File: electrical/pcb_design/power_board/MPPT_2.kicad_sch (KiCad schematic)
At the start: 14 parts

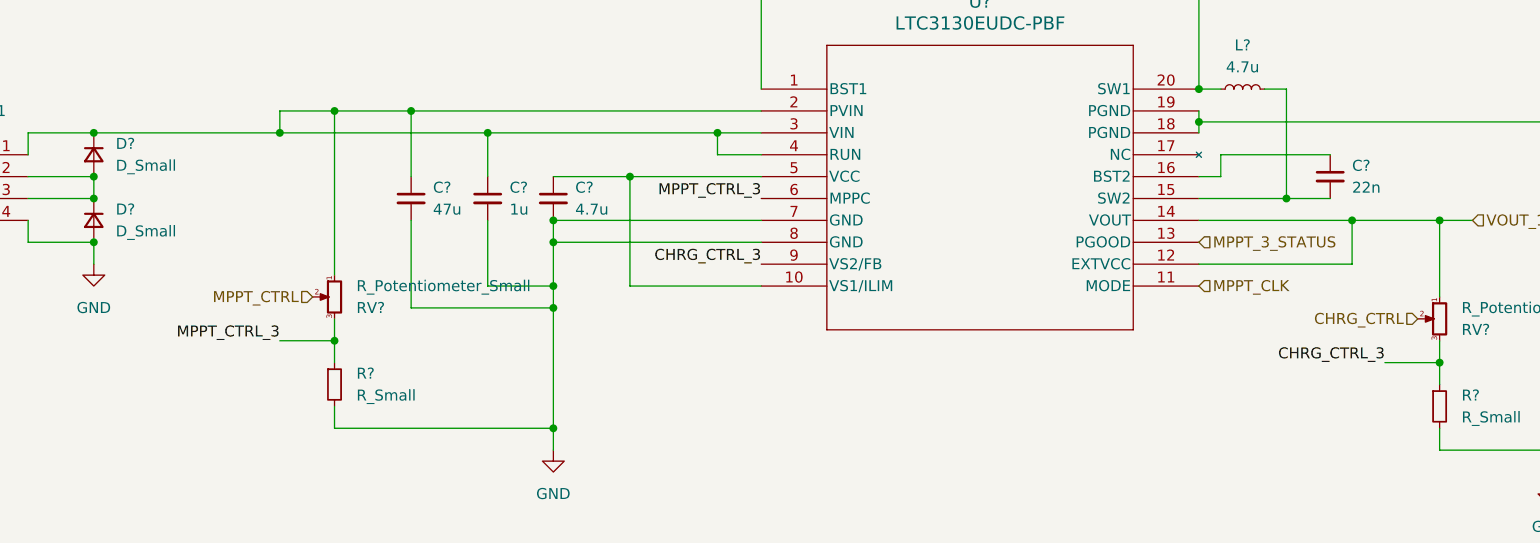
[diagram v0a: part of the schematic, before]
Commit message: missing sense and set hw
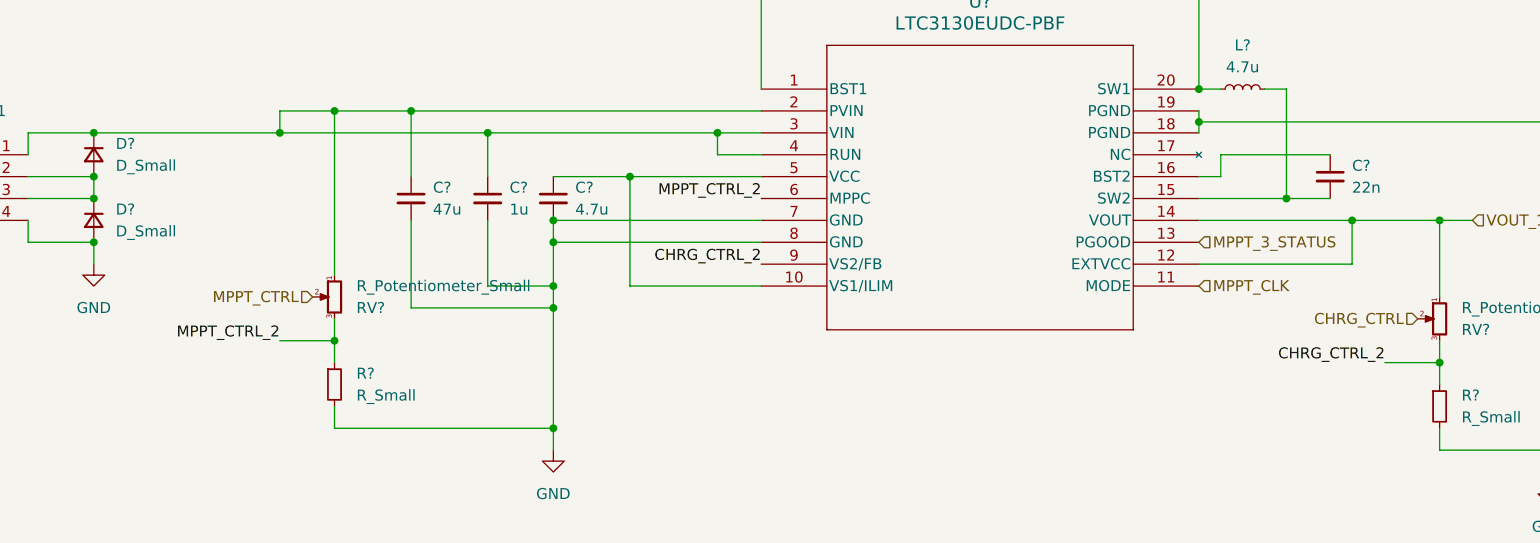
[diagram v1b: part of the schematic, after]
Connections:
- net CHRG_CTRL_3 renamed CHRG_CTRL_2
- net MPPT_CTRL_3 renamed MPPT_CTRL_2

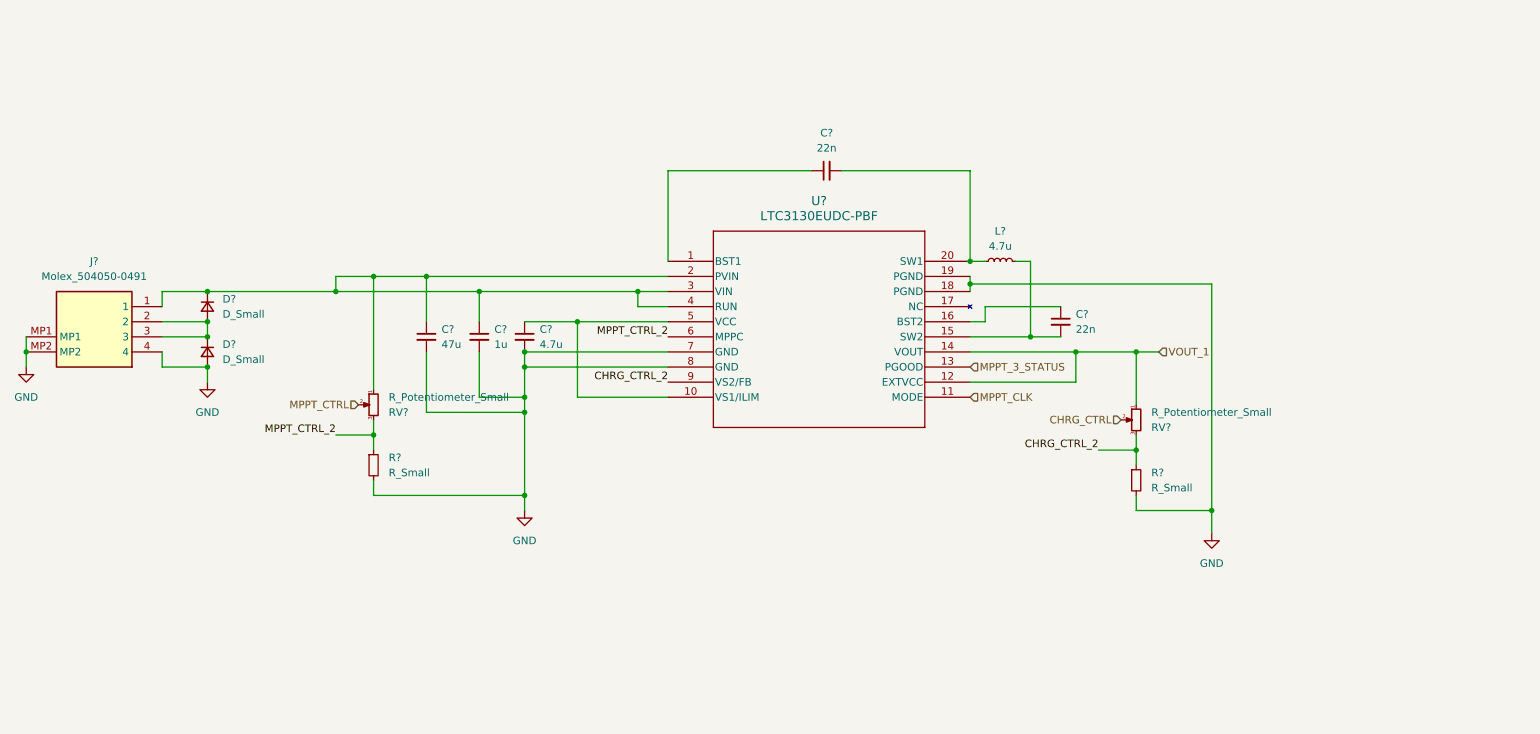
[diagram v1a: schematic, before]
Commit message: power board schematic first draft but missing some resistor and diode specs, and smart mcu pinout
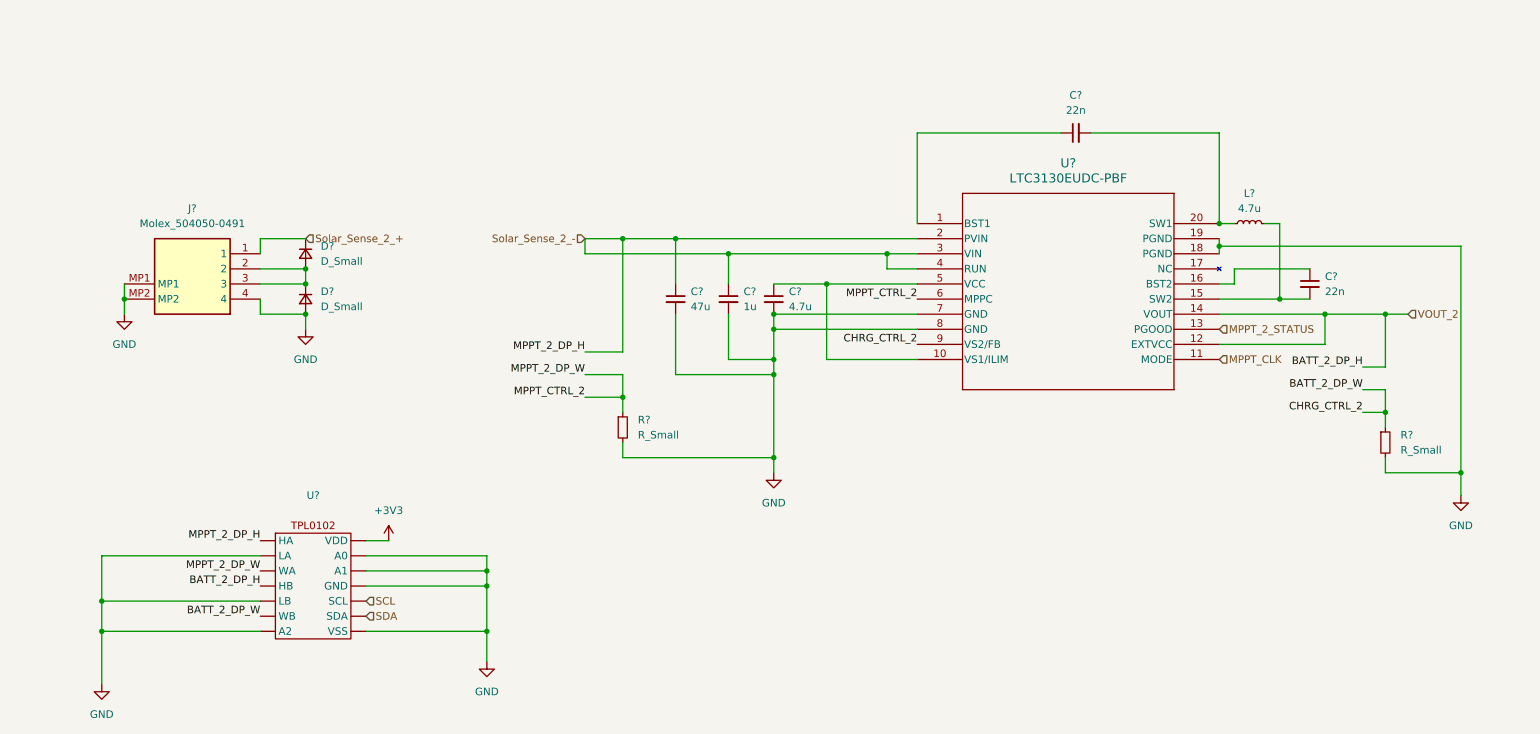
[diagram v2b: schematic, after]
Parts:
- removed C?: 47u, symbol Device:C_Small
- removed C? (x2): 22n, symbol Device:C_Small
- removed C?: 4.7u, symbol Device:C_Small
- removed C?: 1u, symbol Device:C_Small
- removed D? (x2): D_Small, symbol Device:D_Small
- removed J?: Molex_504050-0491, footprints:Molex_504050-0491, symbol tvsc_symbols:Molex_504050-0491
- removed L?: 4.7u, symbol Device:L_Small
- removed R? (x2): R_Small, symbol Device:R_Small
- removed RV? (x2): R_Potentiometer_Small, symbol Device:R_Potentiometer_Small
- removed U?: LTC3130EUDC-PBF, UDC_20_ADI, symbol LTC3130:LTC3130EUDC-PBF
- added C?: 47u, symbol Device:C_Small
- added C?: 1u, symbol Device:C_Small
- added C? (x2): 22n, symbol Device:C_Small
- added C?: 4.7u, symbol Device:C_Small
- added D? (x2): D_Small, symbol Device:D_Small
- added J?: Molex_504050-0491, footprints:Molex_504050-0491, symbol tvsc_symbols:Molex_504050-0491
- added L?: 4.7u, symbol Device:L_Small
- added R? (x2): R_Small, symbol Device:R_Small
- added U?: ~, symbol power_board_symbols:TPL0102
- added U?: LTC3130EUDC-PBF, UDC_20_ADI, symbol LTC3130:LTC3130EUDC-PBF
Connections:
- net GND: now also C?.2, C?.2, C?.2, D?.2 (A), J?.4, J?.MP1, J?.MP2, R?.2, R?.2, U?. (WB), U?.18 (PGND), U?.19 (PGND), U?.7 (GND), U?.8 (GND)
- net MPPT_CLK: now also U?.11 (MODE)
- new net: D?.1 (K), D?.2 (A), J?.2, J?.3
- new net: C?.2, L?.1, U?.20 (SW1)
- new net: C?.2, L?.2, U?.15 (SW2)
- new net: C?.1, U?.16 (BST2)
- new net: C?.1, U?.1 (BST1)
- new net: C?.1, U?.10 (VS1/ILIM), U?.5 (VCC)
- new net +3V3: U?. (WB)
- new net BATT_2_DP_W: R?.1, U?. (WB), U?.9 (VS2/FB)
- new net MPPT_2_DP_W: R?.1, U?. (WB), U?.6 (MPPC)
- new net MPPT_2_STATUS: U?.13 (PGOOD)
- new net SCL: U?. (WB)
- new net SDA: U?. (WB)
- new net Solar_Sense_2_+: D?.1 (K), J?.1
- new net Solar_Sense_2_-: C?.1, C?.1, U?. (WB), U?.2 (PVIN), U?.3 (VIN), U?.4 (RUN)
- new net VOUT_2: U?. (WB), U?.12 (EXTVCC), U?.14 (VOUT)

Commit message: charger board, digipot on current pins of charger ic, voltage sensing on every side of solar panel
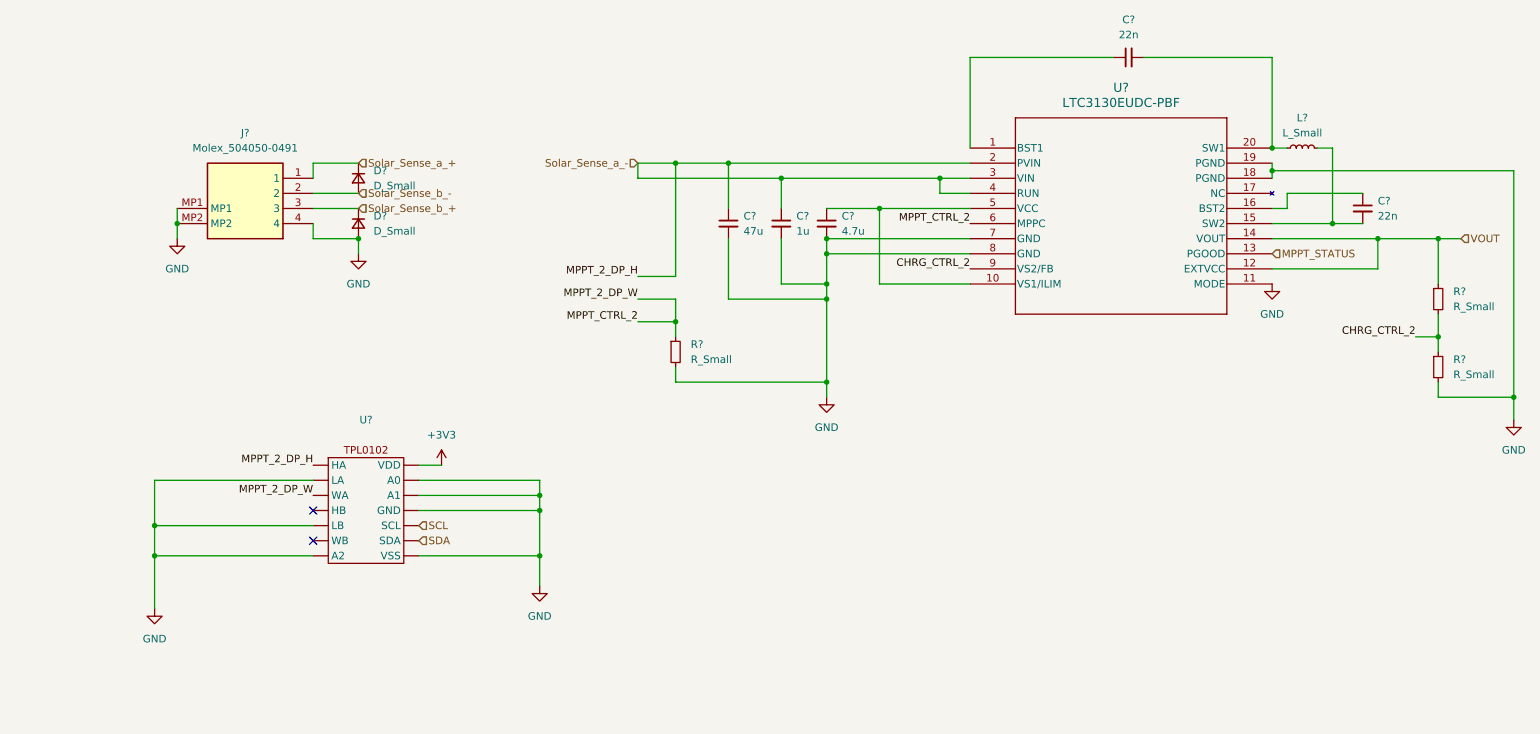
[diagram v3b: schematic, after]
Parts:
- removed C?: 47u, symbol Device:C_Small
- removed C?: 1u, symbol Device:C_Small
- removed C? (x2): 22n, symbol Device:C_Small
- removed C?: 4.7u, symbol Device:C_Small
- removed D? (x2): D_Small, symbol Device:D_Small
- removed J?: Molex_504050-0491, footprints:Molex_504050-0491, symbol tvsc_symbols:Molex_504050-0491
- removed L?: 4.7u, symbol Device:L_Small
- removed R? (x2): R_Small, symbol Device:R_Small
- removed U?: ~, symbol power_board_symbols:TPL0102
- removed U?: LTC3130EUDC-PBF, UDC_20_ADI, symbol LTC3130:LTC3130EUDC-PBF
- added C?: 4.7u, symbol Device:C_Small
- added C? (x2): 22n, symbol Device:C_Small
- added C?: 1u, symbol Device:C_Small
- added C?: 47u, symbol Device:C_Small
- added D? (x2): D_Small, symbol Device:D_Small
- added J?: Molex_504050-0491, footprints:Molex_504050-0491, symbol tvsc_symbols:Molex_504050-0491
- added L?: L_Small, symbol Device:L_Small
- added R? (x3): R_Small, symbol Device:R_Small
- added U?: ~, symbol power_board_symbols:TPL0102
- added U?: LTC3130EUDC-PBF, UDC_20_ADI, symbol LTC3130:LTC3130EUDC-PBF
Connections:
- net +3V3: now also U?. (WB)
- net GND: now also C?.2, C?.2, C?.2, D?.2 (A), J?.4, J?.MP1, J?.MP2, R?.2, R?.2, U?. (WB), U?.11 (MODE), U?.18 (PGND), U?.19 (PGND), U?.7 (GND), U?.8 (GND)
- net MPPT_2_DP_W: now also R?.1, U?. (WB), U?.6 (MPPC)
- net SCL: now also U?. (WB)
- net SDA: now also U?. (WB)
- new net: C?.1, U?.10 (VS1/ILIM), U?.5 (VCC)
- new net: C?.1, U?.16 (BST2)
- new net: C?.2, L?.2, U?.15 (SW2)
- new net: C?.1, U?.1 (BST1)
- new net: C?.2, L?.1, U?.20 (SW1)
- new net CHRG_CTRL_2: R?.1, R?.2, U?.9 (VS2/FB)
- new net MPPT_STATUS: U?.13 (PGOOD)
- new net Solar_Sense_a_+: D?.1 (K), J?.1
- new net Solar_Sense_a_-: C?.1, C?.1, U?. (WB), U?.2 (PVIN), U?.3 (VIN), U?.4 (RUN)
- new net Solar_Sense_b_+: D?.1 (K), J?.3
- new net Solar_Sense_b_-: D?.2 (A), J?.2
- new net VOUT: R?.1, U?.12 (EXTVCC), U?.14 (VOUT)
- no-connect marks 0 -> 2
